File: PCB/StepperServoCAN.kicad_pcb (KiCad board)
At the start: 2 copper layers, 56 x 42.8 mm, 134 parts, among them J1 Debug, J2 CAR, J3 Motor, J4 Conn_01x02, Q1 BSS84, SW1 Rst, SW2 Fcn>, SW3 Fcn>, U1 XL1509-adj, U2 STM32F103CBT6, U3 LMV321, U4 A4950E, U5 A4950E, U6 LMV321, U7 TLE5012B, U8 SN65HVD230, Y1 16Mhz 9pF

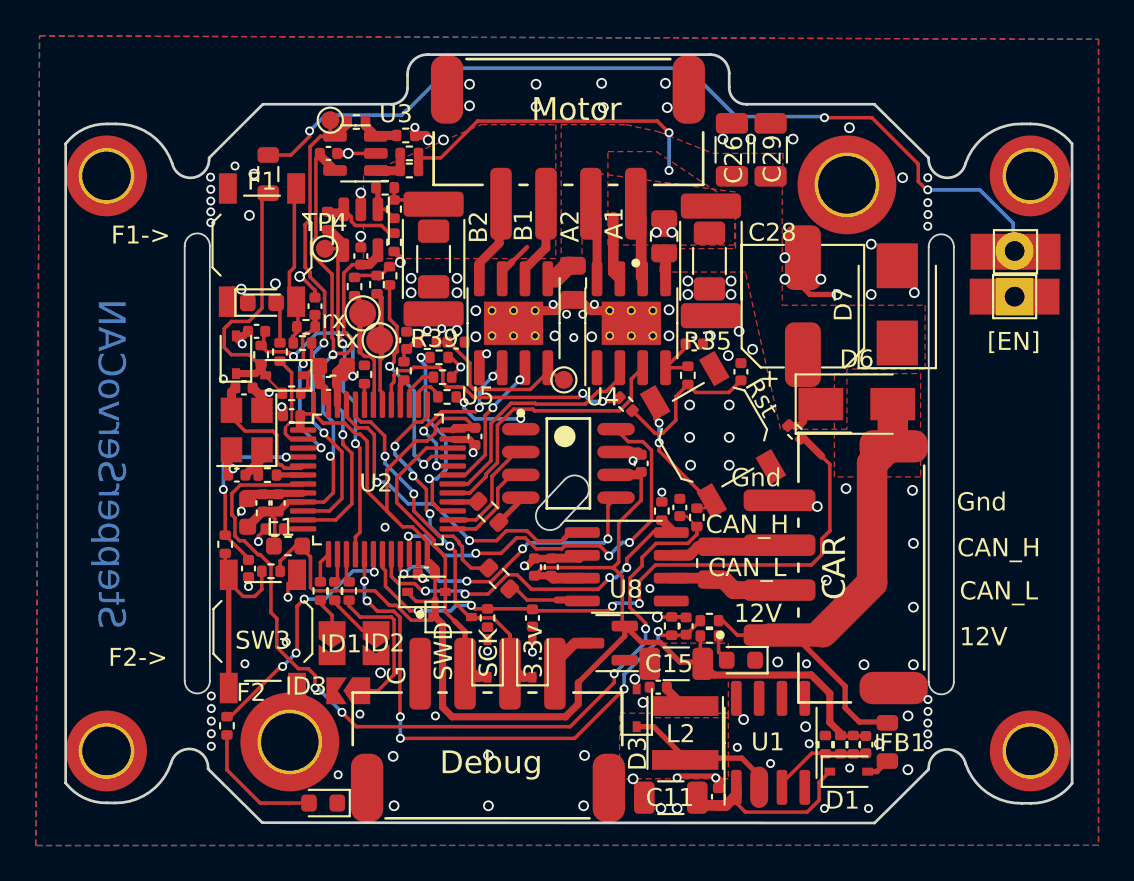
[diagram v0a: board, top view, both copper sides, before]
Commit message: Removed sense resitor 2512 spare footprint. Board widened by 0.4mm
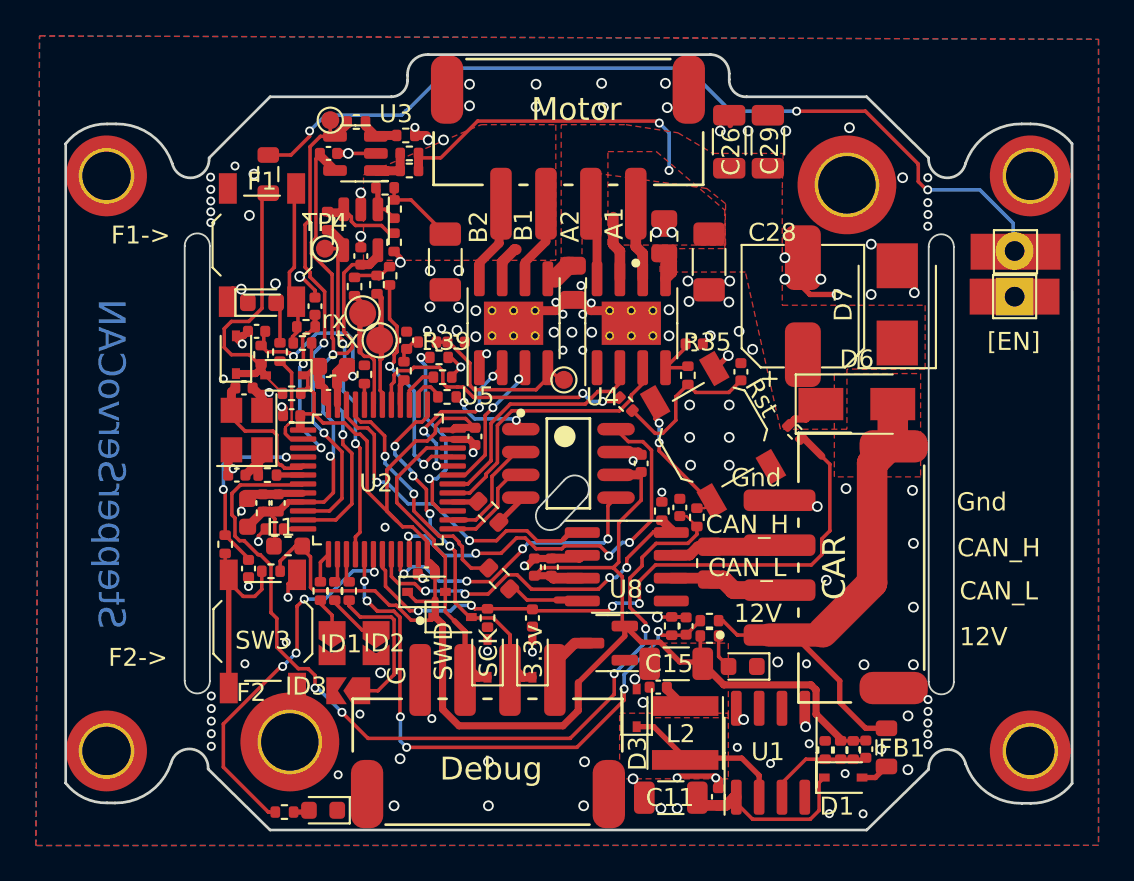
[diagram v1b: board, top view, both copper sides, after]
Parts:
- removed R210, R240: 0.1R, Resistor_SMD:R_2512_6332Metric_Pad1.40x3.35mm_HandSolder
- moved R12 5.77 mm to (84.2, 119.4), turned to 180 degrees
- moved R39 0.67 mm to (93.2, 88.8)
- moved U1 0.55 mm to (111.2, 116.1)
- moved C29 0.47 mm to (111.1, 82.1)
- moved C26 0.47 mm to (109.0, 82.1)
- moved D1 0.45 mm to (115.3, 117.5)
- moved D5 0.40 mm to (86.3, 119.3)
- moved D2 0.36 mm to (109.7, 111.3)
- moved J1 0.35 mm to (95.5, 115.1)
- moved FB1 0.30 mm to (117.7, 115.8)
- moved R1 0.30 mm to (114.3, 116.0)
- moved R3 0.30 mm to (115.8, 116.0)
- moved R4 0.30 mm to (115.2, 116.0)
- moved C1 0.25 mm to (116.5, 115.9)
- moved R35 0.06 mm to (107.8, 88.8)
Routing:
- net Net-(U2-PB0): track 14.1 -> 20.8 mm
- net Net-(D5-A): track 7.27 -> 0.89 mm
- net GND: track 48.0 -> 49.1 mm, vias 148 -> 151
- net Net-(U2-NRST): track 49.6 -> 50.5 mm
- net VBATT_ADC: track 31.9 -> 32.8 mm
- net /BATT_Diode: track 10.8 -> 9.99 mm
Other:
- board size 56 x 42.8 mm -> 56 x 43.2 mm

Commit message: Updated footprints from kicad library (rounded pads). Added more small vias for the fets. DRC fixes
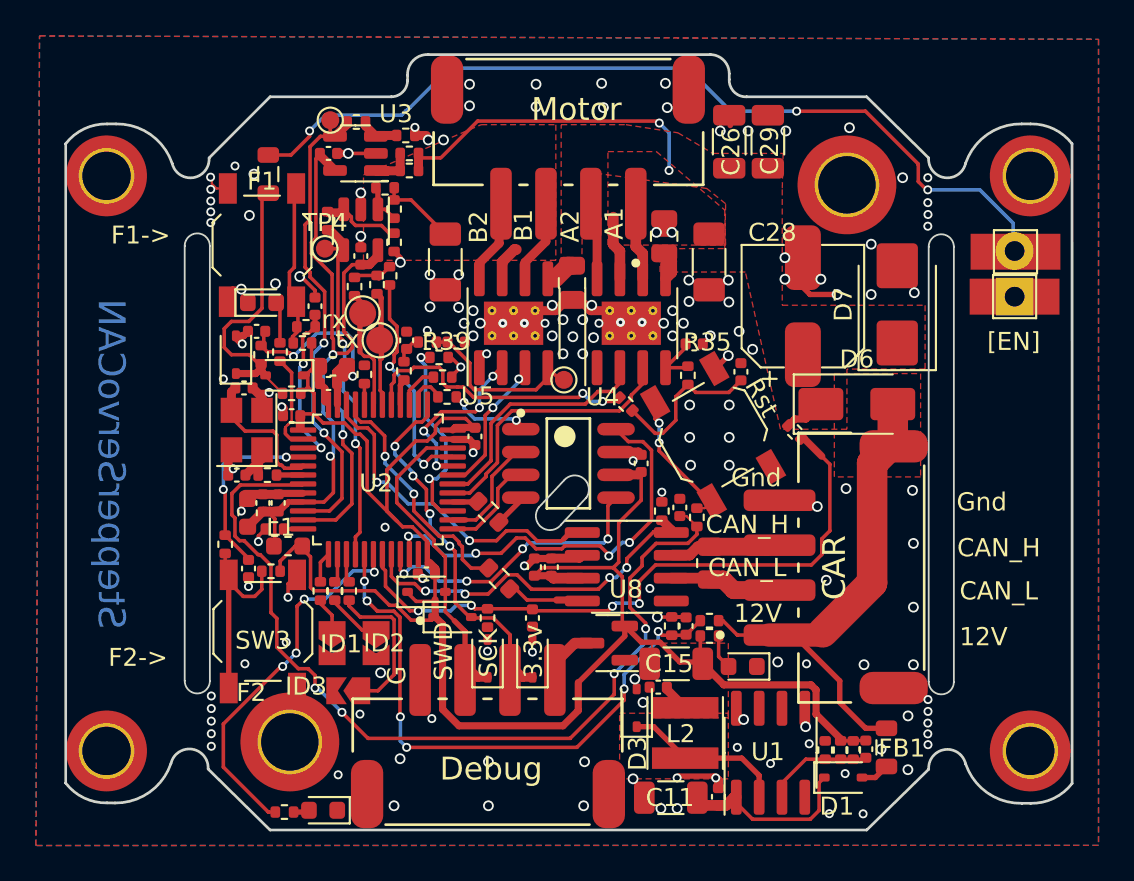
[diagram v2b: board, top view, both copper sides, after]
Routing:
- net GND: track 49.1 -> 50.3 mm, vias 151 -> 158

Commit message: Power lines thickness
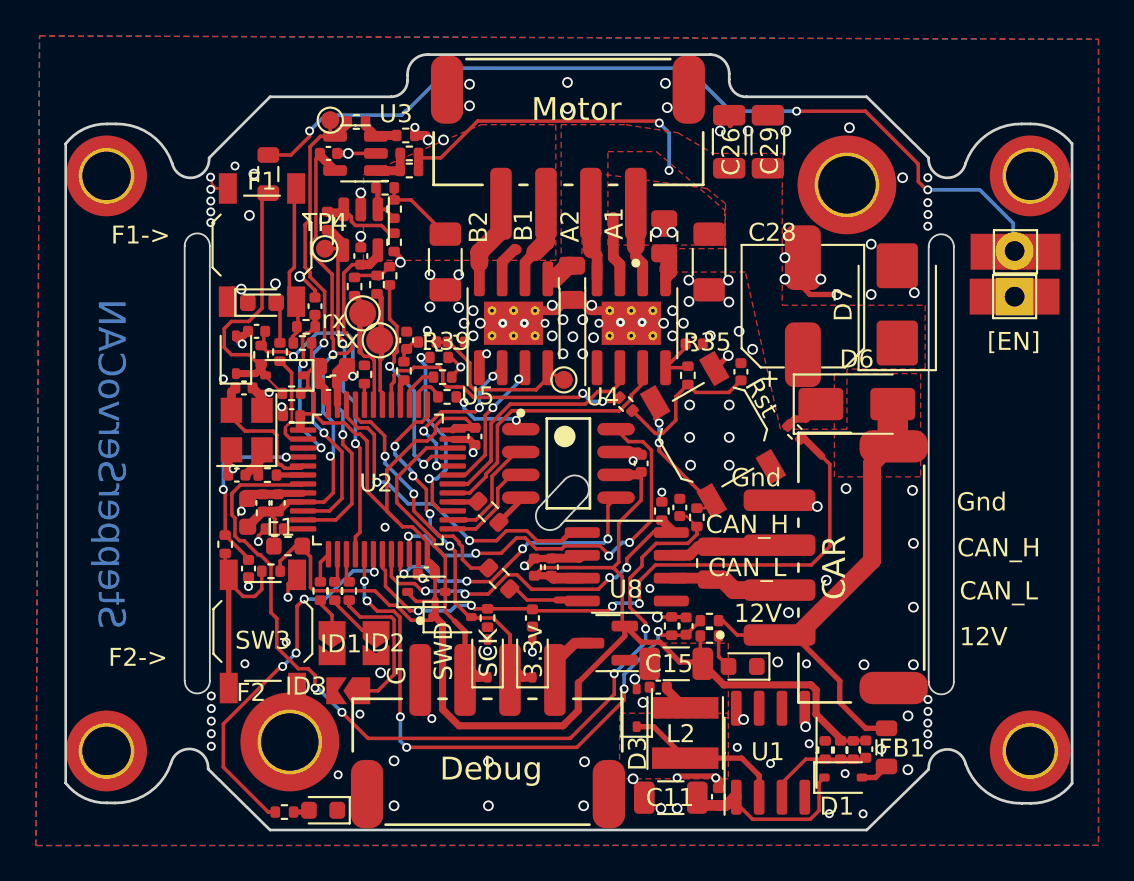
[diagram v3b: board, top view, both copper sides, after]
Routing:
- net +BATT: track 29.2 -> 26.9 mm
- net GND: vias 158 -> 157

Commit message: Replaced 0.2mm tracks with 0.15mm. Removed rx/tx testpoints
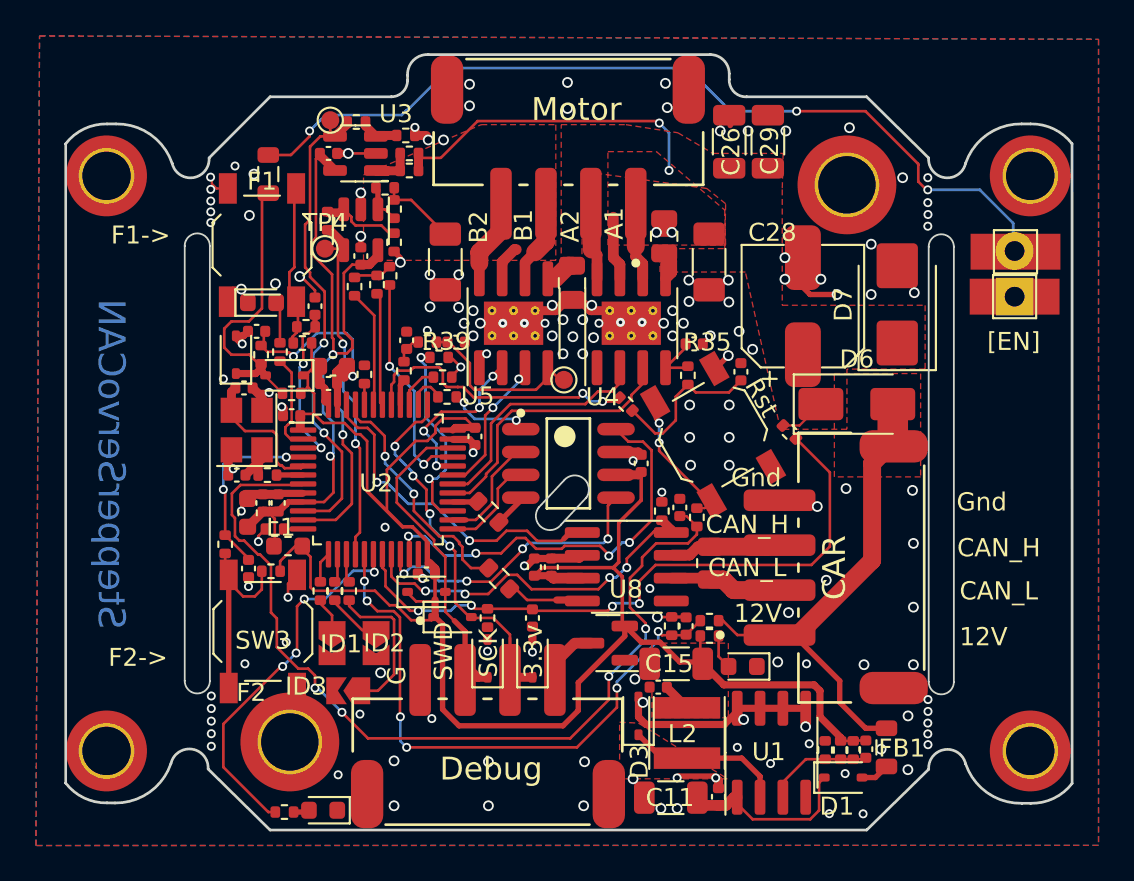
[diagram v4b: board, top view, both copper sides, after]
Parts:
- removed TP1, TP2: WirePad, TestPoint:TestPoint_Pad_D1.5mm
- moved D3 0.46 mm to (103.9, 114.0)
- moved R15 0.30 mm to (112.3, 98.2)
- moved L2 0.10 mm to (106.6, 115.0)
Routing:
- net GND: track 50.3 -> 61.4 mm
- net SWCLK: track 21.9 -> 23.3 mm

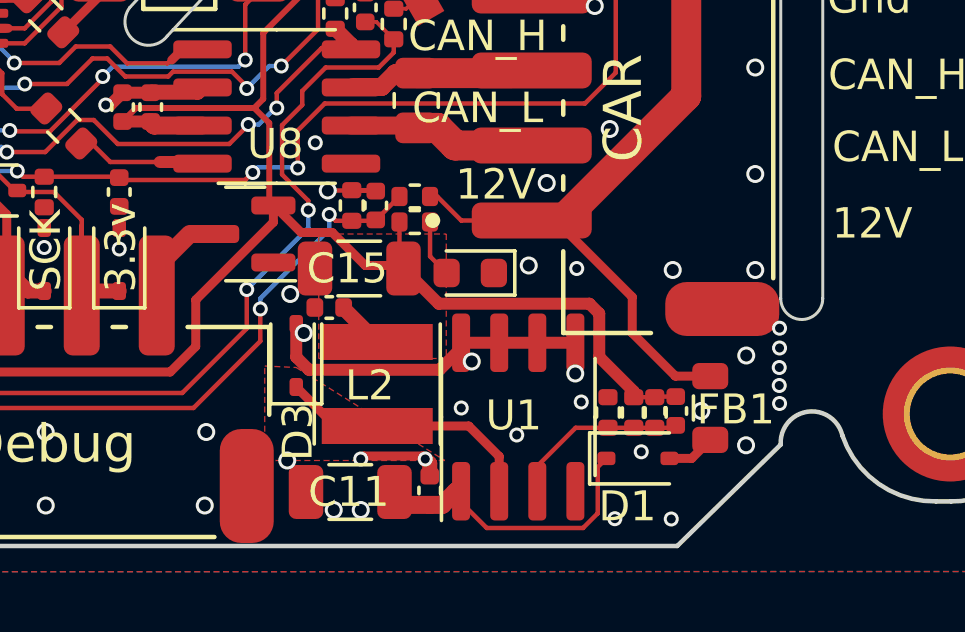
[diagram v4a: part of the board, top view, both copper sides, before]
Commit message: Tighter DCDC off state loop
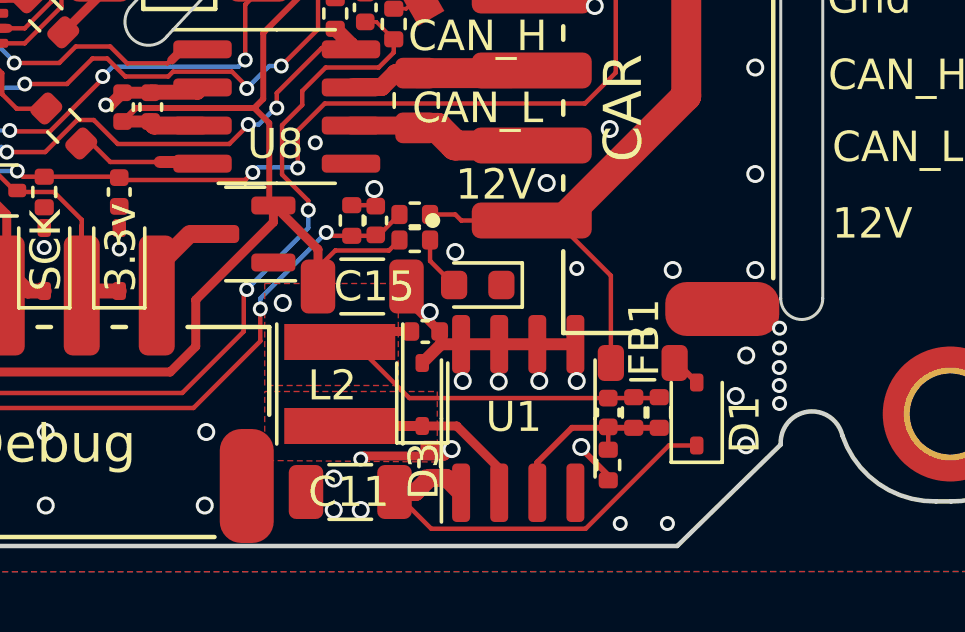
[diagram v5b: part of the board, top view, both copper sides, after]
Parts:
- moved D3 4.40 mm to (108.1, 115.3)
- moved C14 3.30 mm to (108.2, 113.2), turned to 0 degrees
- moved FB1 2.70 mm to (115.5, 114.3), turned to 0 degrees
- moved D1 2.46 mm to (117.2, 116.0), turned to 90 degrees
- moved C1 2.25 mm to (114.3, 116.0)
- moved R1 1.75 mm to (114.3, 117.7), turned to -90 degrees
- moved L2 1.25 mm to (105.3, 115.0)
- moved C12 0.90 mm to (108.3, 117.7)
- moved R4 0.85 mm to (116.0, 116.0)
- moved R3 0.70 mm to (115.2, 116.0)
- moved C15 0.61 mm to (106.1, 111.8), turned to 0 degrees
- moved R5 0.60 mm to (107.8, 110.2)
- moved R16 0.60 mm to (107.8, 109.3)
- moved C19 0.50 mm to (106.5, 109.5)
- moved R22 0.50 mm to (105.8, 109.5)
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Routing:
- net /BATT_Diode: track 10.0 -> 14.4 mm
- net +BATT: track 26.9 -> 24.2 mm
- net Net-(U1-FB): track 6.02 -> 8.03 mm
- net GND: track 61.4 -> 59.5 mm, vias 157 -> 156
- net +3.3V: track 105.0 -> 106.2 mm
- net VBATT_ADC: track 32.8 -> 32.2 mm
- net Net-(D1-A): track 1.62 -> 1.01 mm
- net Net-(D3-K): track 8.88 -> 9.46 mm

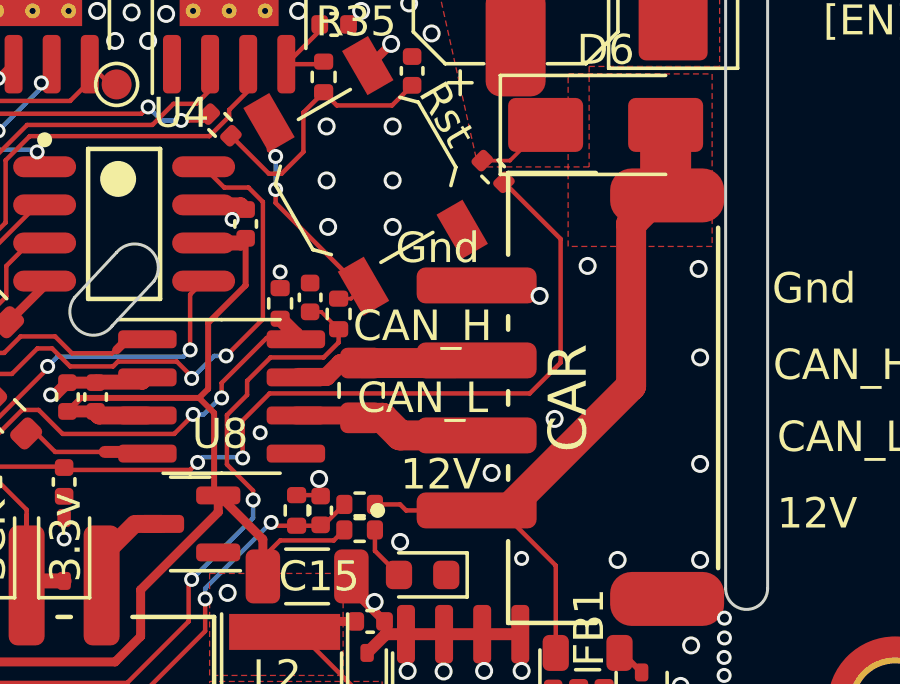
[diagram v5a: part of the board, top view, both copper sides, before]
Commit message: Added solder jumper for CAN terminator resistor
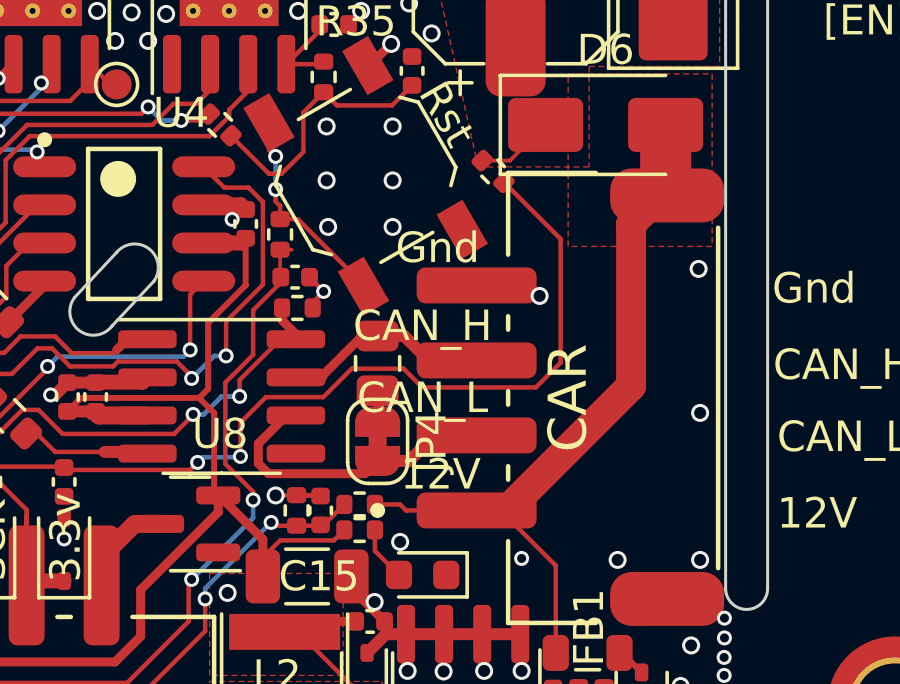
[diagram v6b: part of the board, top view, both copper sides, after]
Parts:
- added JP4: SolderJumper_2_Bridged, Jumper:SolderJumper-2_P1.3mm_Bridged_RoundedPad1.0x1.5mm, F.Cu at (108.5, 107.2)
- moved R2 3.29 mm to (105.2, 100.3)
- moved R46 1.05 mm to (108.5, 104.7)
- moved C10 0.84 mm to (105.7, 101.8), turned to 0 degrees
- moved R47 0.59 mm to (105.8, 102.8), turned to 180 degrees
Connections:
- R46 pad 2: CAN_L -> Net-(JP4-A)
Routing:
- net CAN_L: track 5.74 -> 10.2 mm
- net GND: track 59.5 -> 61.9 mm, vias 156 -> 151
- net Net-(JP4-A): track 0.00 -> 1.04 mm
- net CAN_H: track 5.59 -> 6.33 mm
- net Net-(R2-Pad2): track 7.85 -> 7.11 mm

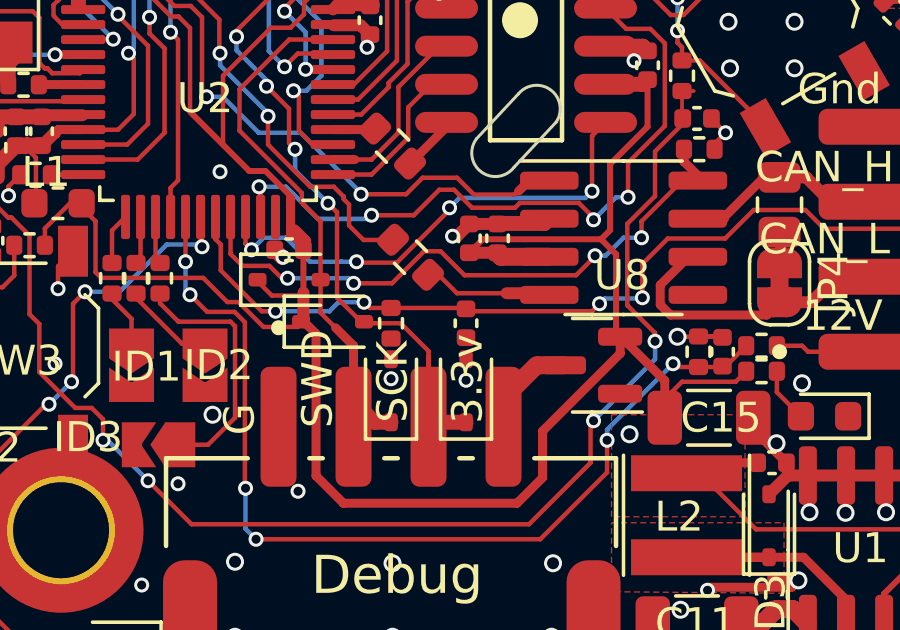
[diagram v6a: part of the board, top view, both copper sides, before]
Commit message: Added overvoltage protection to Vmot adc
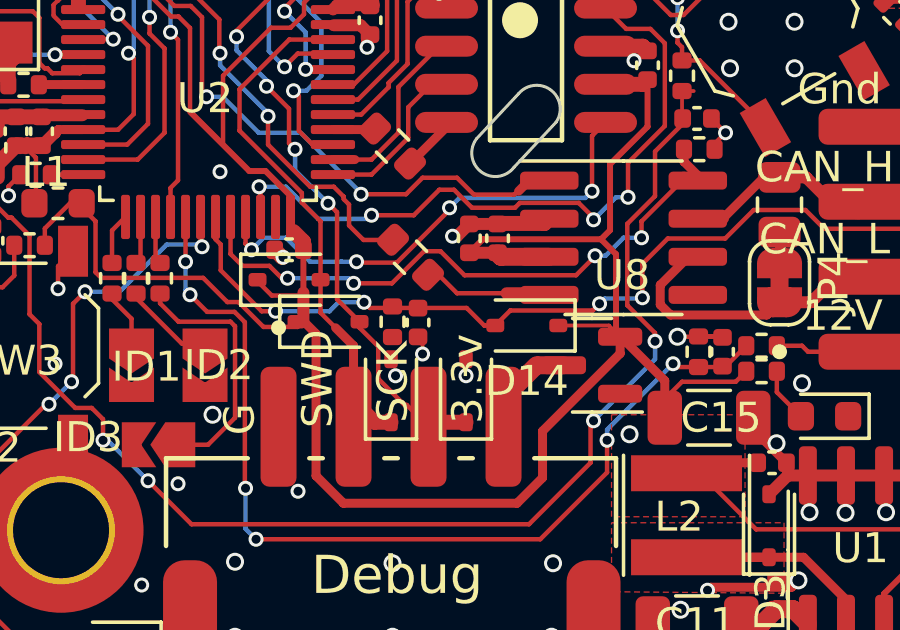
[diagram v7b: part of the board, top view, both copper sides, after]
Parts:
- added D14: 1N5819WS, Diode_SMD:D_SOD-323, F.Cu at (100.0, 108.7)
- moved C18 1.60 mm to (96.4, 108.6)
- moved D10 0.15 mm to (93.4, 108.5)
- moved R21 0.07 mm to (95.5, 108.5)
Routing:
- net SWCLK: track 23.3 -> 20.3 mm
- net +3.3V: track 106.2 -> 108.4 mm
- net GND: track 61.9 -> 62.5 mm, vias 151 -> 152
